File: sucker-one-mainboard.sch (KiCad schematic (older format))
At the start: 72 parts

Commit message: schematics finished
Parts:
- added C21: 4700uF 16v, symbol Device:C
- added J12: Conn_01x06_Male, symbol Connector:Conn_01x06_Male
- added J13, J9: UART1, symbol Connector:Conn_01x04_Male
- added J14: SPI1, symbol Connector:Conn_01x06_Male
- added J5: VBUS, symbol Connector:Conn_01x02_Male
- added J6: +12V, symbol Connector:Conn_01x02_Male
- added J7: 3v3, symbol Connector:Conn_01x02_Male
- added J8: GND, symbol Connector:Conn_01x02_Male
- added TP1: TP USB D+, symbol Connector:TestPoint
- added TP10: TP +12V, symbol Connector:TestPoint
- added TP11: TP 3v3, symbol Connector:TestPoint
- added TP12: TP VBUS, symbol Connector:TestPoint
- added TP13: TP GND, symbol Connector:TestPoint
- added TP14: TP UART1 RX, symbol Connector:TestPoint
- added TP15: TP UART1 TX, symbol Connector:TestPoint
- added TP16: TP I2C1_SDA, symbol Connector:TestPoint
- added TP17: TP Pump +, symbol Connector:TestPoint
- added TP18: TP Pump -, symbol Connector:TestPoint
- added TP19: TP I2C1_SCL, symbol Connector:TestPoint
- added TP2: TP USB D-, symbol Connector:TestPoint
- added TP20: TP UART2 RX, symbol Connector:TestPoint
- added TP21: TP UART2 TX, symbol Connector:TestPoint
- added TP22: TP JTCK, symbol Connector:TestPoint
- added TP23: TP JTMS, symbol Connector:TestPoint
- added TP24: TP JTDO, symbol Connector:TestPoint
- added TP25: TP SPI1 CS, symbol Connector:TestPoint
- added TP26: TP SPI1 CLK, symbol Connector:TestPoint
- added TP27: TP SPI1 MISO, symbol Connector:TestPoint
- added TP28: TP SPI1 MOSI, symbol Connector:TestPoint
- added TP29: TP BOOT1, symbol Connector:TestPoint
- added TP3: TP NC Valve +, symbol Connector:TestPoint
- added TP30: TP BOOT0, symbol Connector:TestPoint
- added TP4: TP NC Valve -, symbol Connector:TestPoint
- added TP5: TP NRST, symbol Connector:TestPoint
- added TP6: TP NO Valve +, symbol Connector:TestPoint
- added TP7: TP NO Valve -, symbol Connector:TestPoint
- added TP8: TP 3 Way Valve +, symbol Connector:TestPoint
- added TP9: TP 3 Way Valve -, symbol Connector:TestPoint
- gave numbers to parts that had none: 72
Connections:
- wire segments 314 -> 382
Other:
- note added: "Aux"
- note added: "BOOT"
- note added: "Programming Interface"
- note added: "SPI"
- note added: "UART"
- moved on the sheet: D2, D3, J1, J10, Q1, Q4, R16, R18, R6, R8, SOD3

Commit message: schematics done
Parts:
- removed C21: 4700uF 16v, symbol Device:C
- removed J3: AudioJack3, symbol Connector:AudioJack3
- added C21: 330uF 35v, Capacitor_SMD:CP_Elec_10x10, symbol Device:CP
- added C22: 0.1uF, Capacitor_SMD:C_0603_1608Metric_Pad1.08x0.95mm_HandSolder, symbol Device:C
- added J15: FOOTPEDAL, Connector_PinHeader_2.54mm:PinHeader_1x03_P2.54mm_Vertical, symbol Connector:Conn_01x03_Male
- added J3: 6P4C, Connector_RJ:RJ14_Connfly_DS1133-S4_Horizontal, symbol Connector:6P4C
- added R19, R20, R21: 5k (OPTIONAL), Resistor_SMD:R_0603_1608Metric_Pad0.98x0.95mm_HandSolder, symbol Device:R
- added RV1, RV2: 10k, Potentiometer_SMD:Potentiometer_Bourns_3314J_Vertical, symbol Device:R_POT
- added TP31: TP FOOTPEDAL, TestPoint:TestPoint_Pad_D2.0mm, symbol Connector:TestPoint
- added TP32: TP VACSENSE, TestPoint:TestPoint_Pad_D2.0mm, symbol Connector:TestPoint
- added TP33: TP FOOTPEDAL AUX, TestPoint:TestPoint_Pad_D2.0mm, symbol Connector:TestPoint
- added U4: 2SMPP-03, 2SMPP-03:XDCR_2SMPP-03, symbol 2SMPP-03:2SMPP-03
- added U5: INA125UA, INA125UA:SOIC127P600X175-16N, symbol INA125UA:INA125UA
- C1, C10, C12, C13, C14, C17, C18, C19, C2, C20, C3, C4, C5, C6, C7, C8, C9: footprint (none) -> Capacitor_SMD:C_0603_1608Metric_Pad1.08x0.95mm_HandSolder
- C11: value 10n -> 10u; footprint (none) -> Capacitor_SMD:C_0603_1608Metric_Pad1.08x0.95mm_HandSolder
- C15, C16: footprint (none) -> Capacitor_SMD:C_1206_3216Metric_Pad1.33x1.80mm_HandSolder
- D1: footprint (none) -> Diode_SMD:D_SMA
- D10: renamed from SOD2; footprint (none) -> Diode_SMD:D_SOD-123F
- D11: renamed from SOD3; footprint (none) -> Diode_SMD:D_SOD-123F
- D2, D7, D8: footprint (none) -> LED_SMD:LED_0603_1608Metric_Pad1.05x0.95mm_HandSolder
- D3: footprint (none) -> Diode_SMD:D_SOD-123F
- D4, D5, D6: footprint DIO_TPD1E05U06DPYR -> TPD1E05U06DPYR:DIO_TPD1E05U06DPYR
- D9: renamed from SOD1; footprint (none) -> Diode_SMD:D_SOD-123F
- F1: value 1210L150THWR -> 1812L075PR; footprint (none) -> Fuse:Fuse_1210_3225Metric_Pad1.42x2.65mm_HandSolder
- F2: footprint (none) -> Fuse:Fuse_1812_4532Metric_Pad1.30x3.40mm_HandSolder
- FB1: footprint (none) -> Inductor_SMD:L_0603_1608Metric_Pad1.05x0.95mm_HandSolder
- J1, J10, J2, J4: footprint (none) -> Connector_JST:JST_XH_B2B-XH-A_1x02_P2.50mm_Vertical
- J11: footprint (none) -> Connector_JST:JST_XH_B5B-XH-A_1x05_P2.50mm_Vertical
- J12: value Conn_01x06_Male -> SWD; footprint (none) -> Connector_PinHeader_2.54mm:PinHeader_1x06_P2.54mm_Vertical
- J13, J9: footprint (none) -> Connector_PinHeader_2.54mm:PinHeader_1x04_P2.54mm_Vertical
- J14: footprint (none) -> Connector_PinHeader_2.54mm:PinHeader_1x06_P2.54mm_Vertical
- J5, J6, J7, J8: footprint (none) -> Connector_PinHeader_2.54mm:PinHeader_1x02_P2.54mm_Vertical
- JP1: footprint (none) -> Jumper:SolderJumper-2_P1.3mm_Bridged_Pad1.0x1.5mm
- JP2: footprint (none) -> Jumper:SolderJumper-2_P1.3mm_Open_Pad1.0x1.5mm
- L1: footprint (none) -> Inductor_SMD:SMD,5.0x5.0x4.0mm
- Q4: value MMBF170LT1G -> DMN15H310SE-13
- R1, R10, R11, R12, R13, R14, R15, R16, R17, R18, R2, R3, R4, R5, R6, R7, R8, R9: footprint (none) -> Resistor_SMD:R_0603_1608Metric_Pad0.98x0.95mm_HandSolder
- SW1: footprint (none) -> TerminalBlock:TerminalBlock_bornier-2_P5.08mm
- SW2: footprint (none) -> Button_Switch_SMD:SW_SPST_B3U-1000P
- TP1, TP10, TP11, TP12, TP13, TP14, TP15, TP16, TP17, TP18, TP19, TP2, TP20, TP21, TP22, TP23, TP24, TP25, TP26, TP27, TP28, TP29, TP3, TP30, TP4, TP5, TP6, TP7, TP8, TP9: footprint (none) -> TestPoint:TestPoint_Pad_D2.0mm
- U2: footprint IC_TPS61087DRCR -> Package_SON:Texas_S-PVSON-N10
- USB1: footprint (none) -> TYPE-C-31-M-12:HRO_TYPE-C-31-M-12
- Y1: footprint (none) -> Crystal:Crystal_SMD_5032-2Pin_5.0x3.2mm
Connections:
- net labels added: FOOTPEDAL_AUX, IAREF, VACSENSE
- wire segments 382 -> 447
- no-connect marks 29 -> 31
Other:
- note added: "Vacuum Sensor"
- moved on the sheet: J11, J12, JP1, JP2, R13, R14, R15, R17, TP10, TP11, TP12, TP16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

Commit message: wip
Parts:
- removed J13, J9: UART1, Connector_PinHeader_2.54mm:PinHeader_1x04_P2.54mm_Vertical, symbol Connector:Conn_01x04_Male
- removed J14: SPI1, Connector_PinHeader_2.54mm:PinHeader_1x06_P2.54mm_Vertical, symbol Connector:Conn_01x06_Male
- removed J15: FOOTPEDAL, Connector_PinHeader_2.54mm:PinHeader_1x03_P2.54mm_Vertical, symbol Connector:Conn_01x03_Male
- removed J5: VBUS, Connector_PinHeader_2.54mm:PinHeader_1x02_P2.54mm_Vertical, symbol Connector:Conn_01x02_Male
- removed J6: +12V, Connector_PinHeader_2.54mm:PinHeader_1x02_P2.54mm_Vertical, symbol Connector:Conn_01x02_Male
- removed J7: 3v3, Connector_PinHeader_2.54mm:PinHeader_1x02_P2.54mm_Vertical, symbol Connector:Conn_01x02_Male
- removed J8: GND, Connector_PinHeader_2.54mm:PinHeader_1x02_P2.54mm_Vertical, symbol Connector:Conn_01x02_Male
- removed TP20: TP UART2 RX, TestPoint:TestPoint_Pad_D2.0mm, symbol Connector:TestPoint
- removed TP21: TP UART2 TX, TestPoint:TestPoint_Pad_D2.0mm, symbol Connector:TestPoint
- Q4: footprint Package_TO_SOT_SMD:SOT-23 -> Package_TO_SOT_SMD:SOT-223
- USB1: footprint TYPE-C-31-M-12:HRO_TYPE-C-31-M-12 -> sucker-one-mainboard:HRO-TYPE-C-31-M-12
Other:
- moved on the sheet: TP13, TP25, TP26, TP27, TP28

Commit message: another wip
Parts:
- removed TP33: TP FOOTPEDAL AUX, TestPoint:TestPoint_Pad_D2.0mm, symbol Connector:TestPoint
- added J5: AUX SPI, Connector_JST:JST_XH_B6B-XH-A_1x06_P2.50mm_Vertical, symbol Connector:Conn_01x06_Male
- added J6: AUX I2C, Connector_JST:JST_XH_B4B-XH-A_1x04_P2.50mm_Vertical, symbol Connector:Conn_01x04_Male
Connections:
- net GND: now also U2.11 (EXP), J5.6 (Pin_6), J6.4 (Pin_4)
- net GNDA: no longer U2.11 (EXP)
- net I2C1_SCL: now also J6.3 (Pin_3)
- net I2C1_SDA: now also J6.2 (Pin_2)
- net SPI1_CLK: now also J5.3 (Pin_3)
- net SPI1_CS: now also J5.2 (Pin_2)
- net SPI1_MISO: now also J5.4 (Pin_4)
- net SPI1_MOSI: now also J5.5 (Pin_5)
- net VDD: now also J5.1 (Pin_1), J6.1 (Pin_1)
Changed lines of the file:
@@
 	4200 6700 4200 6750
-$Comp
-L power:GNDA #PWR0128
-U 1 1 60109EFB
-P 6100 6200
-F 0 "#PWR0128" H 6100 5950 50  0001 C CNN
-F 1 "GNDA" H 6105 6027 50  0000 C CNN
-F 2 "" H 6100 6200 50  0001 C CNN
-F 3 "" H 6100 6200 50  0001 C CNN
-	1    6100 6200
-	1    0    0    -1
-$EndComp
-Wire Wire Line
-	6100 6100 6100 6200
-Wire Wire Line
-	5750 6100 6100 6100
 $Comp
 L Device:L L1
@@
 Wire Wire Line
 	7450 5300 7350 5300
-$Comp
-L Connector:TestPoint TP33
-U 1 1 615D2268
-P 7500 5900
-F 0 "TP33" V 7500 6100 50  0000 L CNN
-F 1 "TP FOOTPEDAL AUX" V 7600 5750 50  0000 L CNN
-F 2 "TestPoint:TestPoint_Pad_D2.0mm" H 7700 5900 50  0001 C CNN
-F 3 "~" H 7700 5900 50  0001 C CNN
-	1    7500 5900
-	0    1    1    0
-$EndComp
-Text GLabel 7350 5900 0    50   Input ~ 0
-FOOTPEDAL_AUX
-Wire Wire Line
-	7350 5900 7500 5900
 Wire Wire Line
 	650  2150 650  2500
@@
 	14000 1200 14100 1200
 Connection ~ 14100 1200
+Text GLabel 8500 8900 2    50   Input ~ 0
+SPI1_CS
+Text GLabel 8500 9000 2    50   Input ~ 0
+SPI1_CLK
+Text GLabel 8500 9100 2    50   Input ~ 0
+SPI1_MISO
+Text GLabel 8500 9200 2    50   Input ~ 0
+SPI1_MOSI
+$Comp
+L power:GND #PWR0156
+U 1 1 5FE7577B
+P 8500 9350
+F 0 "#PWR0156" H 8500 9100 50  0001 C CNN
+F 1 "GND" H 8505 9177 50  0000 C CNN
+F 2 "" H 8500 9350 50  0001 C CNN
+F 3 "" H 8500 9350 50  0001 C CNN
+	1    8500 9350
+	1    0    0    -1
+$EndComp
+$Comp
+L power:VDD #PWR0157
+U 1 1 5FE75B77
+P 8500 8700
+F 0 "#PWR0157" H 8500 8550 50  0001 C CNN
+F 1 "VDD" H 8515 8873 50  0000 C CNN
+F 2 "" H 8500 8700 50  0001 C CNN
+F 3 "" H 8500 8700 50  0001 C CNN
+	1    8500 8700
+	1    0    0    -1
+$EndComp
+$Comp
+L Connector:Conn_01x06_Male J5
+U 1 1 5FEA2D39
+P 7950 9000
+F 0 "J5" H 8058 9381 50  0000 C CNN
+F 1 "AUX SPI" H 8058 9290 50  0000 C CNN
+F 2 "Connector_JST:JST_XH_B6B-XH-A_1x06_P2.50mm_Vertical" H 7950 9000 50  0001 C CNN
+F 3 "~" H 7950 9000 50  0001 C CNN
+	1    7950 9000
+	1    0    0    -1
+$EndComp
+Wire Wire Line
+	8150 8800 8500 8800
+Wire Wire Line
+	8500 8800 8500 8700
+Wire Wire Line
+	8150 8900 8500 8900
+Wire Wire Line
+	8150 9000 8500 9000
+Wire Wire Line
+	8150 9100 8500 9100
+Wire Wire Line
+	8150 9200 8500 9200
+Wire Wire Line
+	8500 9350 8500 9300
+Wire Wire Line
+	8500 9300 8150 9300
+Text GLabel 9850 9150 2    50   Input ~ 0
+I2C1_SCL
+Text GLabel 9850 9050 2    50   Input ~ 0
+I2C1_SDA
+$Comp
+L power:VDD #PWR02
+U 1 1 600C0D50
+P 10250 8550
+F 0 "#PWR02" H 10250 8400 50  0001 C CNN
+F 1 "VDD" H 10265 8723 50  0000 C CNN
+F 2 "" H 10250 8550 50  0001 C CNN
+F 3 "" H 10250 8550 50  0001 C CNN
+	1    10250 8550
+	1    0    0    -1
+$EndComp
+$Comp
+L power:GND #PWR01
+U 1 1 600C0D5C
+P 9950 9350
+F 0 "#PWR01" H 9950 9100 50  0001 C CNN
+F 1 "GND" H 9955 9177 50  0000 C CNN
+F 2 "" H 9950 9350 50  0001 C CNN
+F 3 "" H 9950 9350 50  0001 C CNN
+	1    9950 9350
+	1    0    0    -1
+$EndComp
+Wire Wire Line
+	10250 8950 9600 8950
+Wire Wire Line
+	9850 9050 9600 9050
+Wire Wire Line
+	9850 9150 9600 9150
+Wire Wire Line
+	9950 9350 9950 9250
+Wire Wire Line
+	9950 9250 9600 9250
+Wire Wire Line
+	10250 8550 10250 8950
+$Comp
+L Connector:Conn_01x04_Male J6
+U 1 1 600F1F2E
+P 9400 9050
+F 0 "J6" H 9508 9331 50  0000 C CNN
+F 1 "AUX I2C" H 9508 9240 50  0000 C CNN
+F 2 "Connector_JST:JST_XH_B4B-XH-A_1x04_P2.50mm_Vertical" H 9400 9050 50  0001 C CNN
+F 3 "~" H 9400 9050 50  0001 C CNN
+	1    9400 9050
+	1    0    0    -1
+$EndComp
+Wire Wire Line
+	5750 6100 5900 6100
+Wire Wire Line
+	5900 6100 5900 6200
+Connection ~ 5900 6200
 $EndSCHEMATC

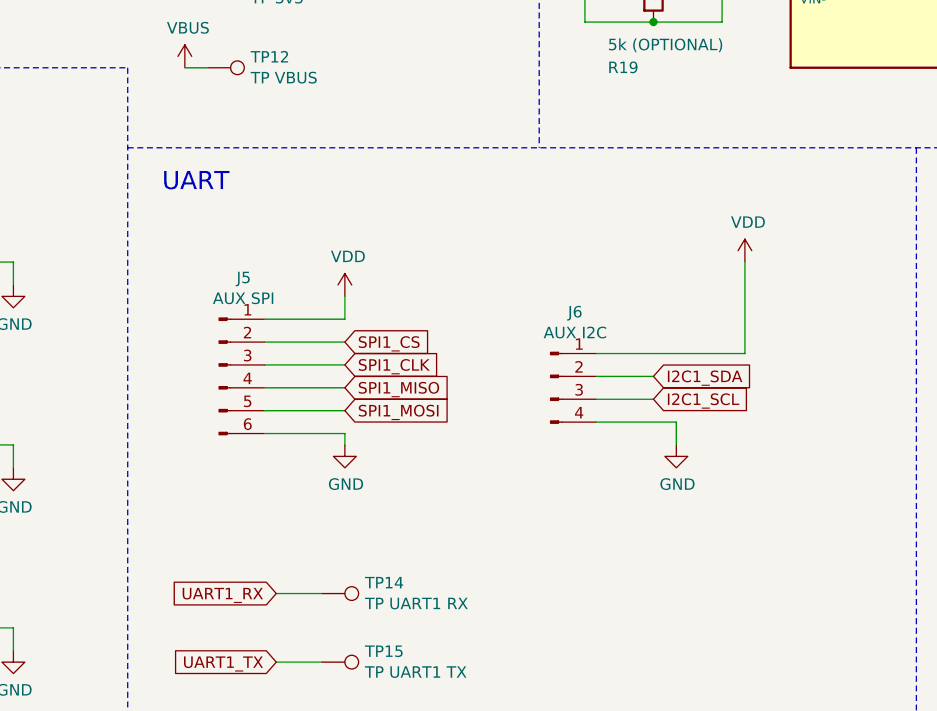
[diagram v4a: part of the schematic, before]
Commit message: added molex
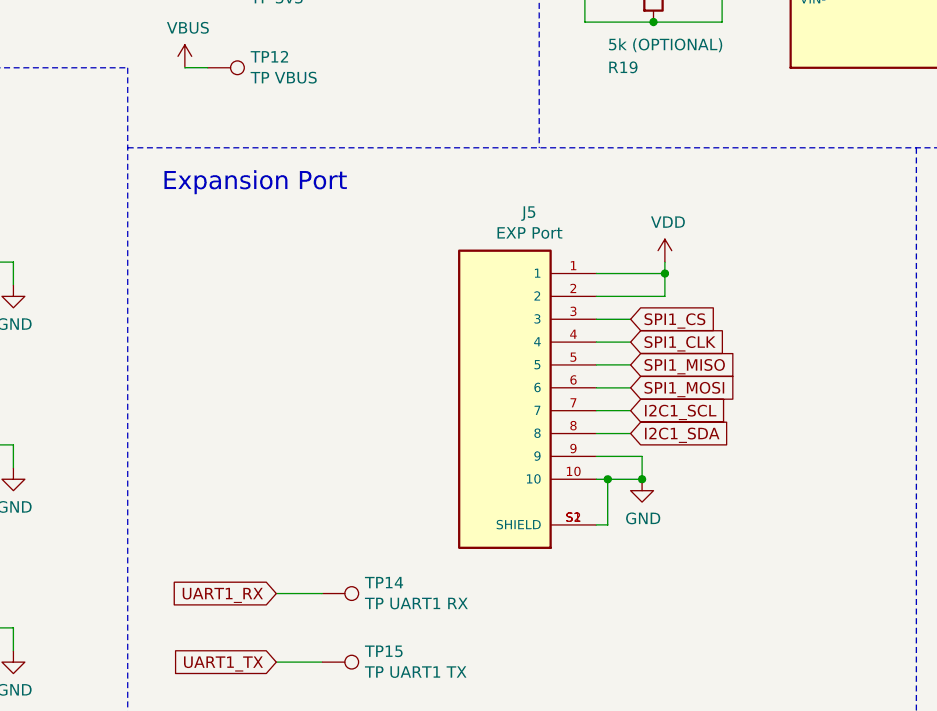
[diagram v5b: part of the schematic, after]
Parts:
- removed J5: AUX SPI, Connector_JST:JST_XH_B6B-XH-A_1x06_P2.50mm_Vertical, symbol Connector:Conn_01x06_Male
- removed J6: AUX I2C, Connector_JST:JST_XH_B4B-XH-A_1x04_P2.50mm_Vertical, symbol Connector:Conn_01x04_Male
- added J5: EXP Port, 5034801000 (2):MOLEX_5034801000, symbol MOLEX_5034801000:5034801000
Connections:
- net GND: now also J5.10, J5.9, J5.S1 (SHIELD), J5.S2 (SHIELD)
- net I2C1_SCL: now also J5.7
- net I2C1_SDA: now also J5.8
- net SPI1_CLK: now also J5.4
- net SPI1_CS: now also J5.3
- net SPI1_MISO: now also J5.5
- net SPI1_MOSI: now also J5.6
- net VDD: now also J5.1, J5.2
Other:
- note added: "Expansion Port"
- note removed: "UART"
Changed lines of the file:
@@
 	8200 10300 8400 10300
 Text Notes 7700 8250 0    79   ~ 0
-UART
+Expansion Port
 Wire Notes Line
 	11000 8050 11000 11200
@@
 	14000 1200 14100 1200
 Connection ~ 14100 1200
-Text GLabel 8500 8900 2    50   Input ~ 0
-SPI1_CS
-Text GLabel 8500 9000 2    50   Input ~ 0
-SPI1_CLK
-Text GLabel 8500 9100 2    50   Input ~ 0
-SPI1_MISO
-Text GLabel 8500 9200 2    50   Input ~ 0
-SPI1_MOSI
-$Comp
-L power:GND #PWR0156
-U 1 1 5FE7577B
-P 8500 9350
-F 0 "#PWR0156" H 8500 9100 50  0001 C CNN
-F 1 "GND" H 8505 9177 50  0000 C CNN
-F 2 "" H 8500 9350 50  0001 C CNN
-F 3 "" H 8500 9350 50  0001 C CNN
-	1    8500 9350
-	1    0    0    -1
-$EndComp
-$Comp
-L power:VDD #PWR0157
-U 1 1 5FE75B77
-P 8500 8700
-F 0 "#PWR0157" H 8500 8550 50  0001 C CNN
-F 1 "VDD" H 8515 8873 50  0000 C CNN
-F 2 "" H 8500 8700 50  0001 C CNN
-F 3 "" H 8500 8700 50  0001 C CNN
-	1    8500 8700
-	1    0    0    -1
-$EndComp
-$Comp
-L Connector:Conn_01x06_Male J5
-U 1 1 5FEA2D39
-P 7950 9000
-F 0 "J5" H 8058 9381 50  0000 C CNN
-F 1 "AUX SPI" H 8058 9290 50  0000 C CNN
-F 2 "Connector_JST:JST_XH_B6B-XH-A_1x06_P2.50mm_Vertical" H 7950 9000 50  0001 C CNN
-F 3 "~" H 7950 9000 50  0001 C CNN
-	1    7950 9000
-	1    0    0    -1
-$EndComp
-Wire Wire Line
-	8150 8800 8500 8800
-Wire Wire Line
-	8500 8800 8500 8700
-Wire Wire Line
-	8150 8900 8500 8900
-Wire Wire Line
-	8150 9000 8500 9000
-Wire Wire Line
-	8150 9100 8500 9100
-Wire Wire Line
-	8150 9200 8500 9200
-Wire Wire Line
-	8500 9350 8500 9300
-Wire Wire Line
-	8500 9300 8150 9300
-Text GLabel 9850 9150 2    50   Input ~ 0
-I2C1_SCL
-Text GLabel 9850 9050 2    50   Input ~ 0
-I2C1_SDA
-$Comp
-L power:VDD #PWR02
-U 1 1 600C0D50
-P 10250 8550
-F 0 "#PWR02" H 10250 8400 50  0001 C CNN
-F 1 "VDD" H 10265 8723 50  0000 C CNN
-F 2 "" H 10250 8550 50  0001 C CNN
-F 3 "" H 10250 8550 50  0001 C CNN
-	1    10250 8550
-	1    0    0    -1
-$EndComp
-$Comp
-L power:GND #PWR01
-U 1 1 600C0D5C
-P 9950 9350
-F 0 "#PWR01" H 9950 9100 50  0001 C CNN
-F 1 "GND" H 9955 9177 50  0000 C CNN
-F 2 "" H 9950 9350 50  0001 C CNN
-F 3 "" H 9950 9350 50  0001 C CNN
-	1    9950 9350
-	1    0    0    -1
-$EndComp
-Wire Wire Line
-	10250 8950 9600 8950
-Wire Wire Line
-	9850 9050 9600 9050
-Wire Wire Line
-	9850 9150 9600 9150
-Wire Wire Line
-	9950 9350 9950 9250
-Wire Wire Line
-	9950 9250 9600 9250
-Wire Wire Line
-	10250 8550 10250 8950
-$Comp
-L Connector:Conn_01x04_Male J6
-U 1 1 600F1F2E
-P 9400 9050
-F 0 "J6" H 9508 9331 50  0000 C CNN
-F 1 "AUX I2C" H 9508 9240 50  0000 C CNN
-F 2 "Connector_JST:JST_XH_B4B-XH-A_1x04_P2.50mm_Vertical" H 9400 9050 50  0001 C CNN
-F 3 "~" H 9400 9050 50  0001 C CNN
-	1    9400 9050
-	1    0    0    -1
-$EndComp
 Wire Wire Line
 	5750 6100 5900 6100
@@
 	5900 6100 5900 6200
 Connection ~ 5900 6200
+Text GLabel 9750 9200 2    50   Input ~ 0
+I2C1_SCL
+Text GLabel 9750 9300 2    50   Input ~ 0
+I2C1_SDA
+Text GLabel 9750 9100 2    50   Input ~ 0
+SPI1_MOSI
+Text GLabel 9750 9000 2    50   Input ~ 0
+SPI1_MISO
+Text GLabel 9750 8900 2    50   Input ~ 0
+SPI1_CLK
+Text GLabel 9750 8800 2    50   Input ~ 0
+SPI1_CS
+Wire Wire Line
+	9600 8800 9750 8800
+Wire Wire Line
+	9600 8900 9750 8900
+Wire Wire Line
+	9600 9000 9750 9000
+Wire Wire Line
+	9600 9100 9750 9100
+Wire Wire Line
+	9600 9200 9750 9200
+Wire Wire Line
+	9600 9300 9750 9300
+$Comp
+L power:GND #PWR01
+U 1 1 604F9A8E
+P 9800 9500
+F 0 "#PWR01" H 9800 9250 50  0001 C CNN
+F 1 "GND" H 9805 9327 50  0000 C CNN
+F 2 "" H 9800 9500 50  0001 C CNN
+F 3 "" H 9800 9500 50  0001 C CNN
+	1    9800 9500
+	1    0    0    -1
+$EndComp
+Wire Wire Line
+	9800 9500 9800 9400
+Wire Wire Line
+	9800 9400 9600 9400
+$Comp
+L power:VDD #PWR02
+U 1 1 60529C0B
+P 9900 8550
+F 0 "#PWR02" H 9900 8400 50  0001 C CNN
+F 1 "VDD" H 9915 8723 50  0000 C CNN
+F 2 "" H 9900 8550 50  0001 C CNN
+F 3 "" H 9900 8550 50  0001 C CNN
+	1    9900 8550
+	1    0    0    -1
+$EndComp
+Wire Wire Line
+	9900 8550 9900 8600
+Wire Wire Line
+	9900 8700 9600 8700
+$Comp
+L MOLEX_5034801000:5034801000 J5
+U 1 1 5FEAB90C
+P 9200 9200
+F 0 "J5" H 9093 10067 50  0000 C CNN
+F 1 "EXP Port" H 9093 9976 50  0000 C CNN
+F 2 "5034801000 (2):MOLEX_5034801000" H 9200 9200 50  0001 L BNN
+F 3 "" H 9200 9200 50  0001 L BNN
+F 4 "MOLEX" H 9200 9200 50  0001 L BNN "MANUFACTURER"
+F 5 "H" H 9200 9200 50  0001 L BNN "PARTREV"
+F 6 "Manufacturer Recommendation" H 9200 9200 50  0001 L BNN "STANDARD"
+	1    9200 9200
+	-1   0    0    -1
+$EndComp
+Wire Wire Line
+	9600 8600 9900 8600
+Connection ~ 9900 8600
+Wire Wire Line
+	9900 8600 9900 8700
+Wire Wire Line
+	9600 9500 9650 9500
+Connection ~ 9800 9500
+Wire Wire Line
+	9600 9700 9650 9700
+Wire Wire Line
+	9650 9700 9650 9500
+Connection ~ 9650 9500
+Wire Wire Line
+	9650 9500 9800 9500
 $EndSCHEMATC

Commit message: last changes and gerber files generated
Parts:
- added D12: TPD1E05U06DPYR, TPD1E05U06DPYR:DIO_TPD1E05U06DPYR, symbol TPD1E05U06DPYR:TPD1E05U06DPYR
- SW1: footprint TerminalBlock:TerminalBlock_bornier-2_P5.08mm -> Connector_JST:JST_XH_B2B-XH-A_1x02_P2.50mm_Vertical
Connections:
- net FOOTPEDAL_AUX: now also D12.1 (I/O)
- net GND: now also D12.2 (GND)
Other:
- moved on the sheet: D6
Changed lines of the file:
@@
 L TPD1E05U06DPYR:TPD1E05U06DPYR D6
 U 1 1 60B9AF26
-P 6050 10250
-F 0 "D6" H 6050 10620 50  0000 C CNN
-F 1 "TPD1E05U06DPYR" H 6050 10529 50  0000 C CNN
-F 2 "TPD1E05U06DPYR:DIO_TPD1E05U06DPYR" H 6050 10250 50  0001 L BNN
-F 3 "" H 6050 10250 50  0001 L BNN
-	1    6050 10250
+P 6050 10150
+F 0 "D6" H 6050 10520 50  0000 C CNN
+F 1 "TPD1E05U06DPYR" H 6050 10429 50  0000 C CNN
+F 2 "TPD1E05U06DPYR:DIO_TPD1E05U06DPYR" H 6050 10150 50  0001 L BNN
+F 3 "" H 6050 10150 50  0001 L BNN
+	1    6050 10150
 	1    0    0    -1
 $EndComp
@@
 L power:GND #PWR0147
 U 1 1 60C1BC19
-P 7050 10250
-F 0 "#PWR0147" H 7050 10000 50  0001 C CNN
-F 1 "GND" H 7055 10077 50  0000 C CNN
-F 2 "" H 7050 10250 50  0001 C CNN
-F 3 "" H 7050 10250 50  0001 C CNN
-	1    7050 10250
-	1    0    0    -1
-$EndComp
-Wire Wire Line
-	6750 10150 7050 10150
-Wire Wire Line
-	7050 10150 7050 10250
+P 7050 10150
+F 0 "#PWR0147" H 7050 9900 50  0001 C CNN
+F 1 "GND" H 7055 9977 50  0000 C CNN
+F 2 "" H 7050 10150 50  0001 C CNN
+F 3 "" H 7050 10150 50  0001 C CNN
+	1    7050 10150
+	1    0    0    -1
+$EndComp
+Wire Wire Line
+	6750 10050 7050 10050
+Wire Wire Line
+	7050 10050 7050 10150
 Text GLabel 5150 9350 0    39   Input ~ 0
 D-
 Wire Wire Line
 	5150 9350 5350 9350
-Text GLabel 5150 10150 0    39   Input ~ 0
+Text GLabel 5150 10050 0    39   Input ~ 0
 D+
 Wire Wire Line
-	5150 10150 5350 10150
+	5150 10050 5350 10050
 Wire Notes Line
 	7550 7700 7550 11200
@@
 F 0 "SW1" H 2600 8535 50  0000 C CNN
 F 1 "Power Switch" H 2600 8444 50  0000 C CNN
-F 2 "TerminalBlock:TerminalBlock_bornier-2_P5.08mm" H 2600 8300 50  0001 C CNN
+F 2 "Connector_JST:JST_XH_B2B-XH-A_1x02_P2.50mm_Vertical" H 2600 8300 50  0001 C CNN
 F 3 "~" H 2600 8300 50  0001 C CNN
 	1    2600 8300
@@
 Wire Wire Line
 	9650 9500 9800 9500
+$Comp
+L TPD1E05U06DPYR:TPD1E05U06DPYR D12
+U 1 1 6008F82D
+P 6050 10850
+F 0 "D12" H 6050 11220 50  0000 C CNN
+F 1 "TPD1E05U06DPYR" H 6050 11129 50  0000 C CNN
+F 2 "TPD1E05U06DPYR:DIO_TPD1E05U06DPYR" H 6050 10850 50  0001 L BNN
+F 3 "" H 6050 10850 50  0001 L BNN
+	1    6050 10850
+	1    0    0    -1
+$EndComp
+$Comp
+L power:GND #PWR011
+U 1 1 600BEC9A
+P 7050 10900
+F 0 "#PWR011" H 7050 10650 50  0001 C CNN
+F 1 "GND" H 7055 10727 50  0000 C CNN
+F 2 "" H 7050 10900 50  0001 C CNN
+F 3 "" H 7050 10900 50  0001 C CNN
+	1    7050 10900
+	1    0    0    -1
+$EndComp
+Wire Wire Line
+	6750 10750 7050 10750
+Wire Wire Line
+	7050 10750 7050 10900
+Text GLabel 5150 10750 0    50   Input ~ 0
+FOOTPEDAL_AUX
+Wire Wire Line
+	5150 10750 5350 10750
 $EndSCHEMATC
